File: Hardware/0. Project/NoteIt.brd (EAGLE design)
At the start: 160 x 100 mm, 64 parts, among them CN2 MicroSD Card, CN3 MicroSD Card, CN7 1x4, IC2 MCP73831/2, IC5 S-8261ACMMD-G4MT2U, Q2 SI2374DS, Q3 SI2374DS, Q4 BC817, SW1 KY-040, U10 MSP430FR2476TPTR, U5 TLV75530PDBVR, U6 GL823, U8 ADG774, U9 ADG774, X2 32.768 kHz, X3 microUSB

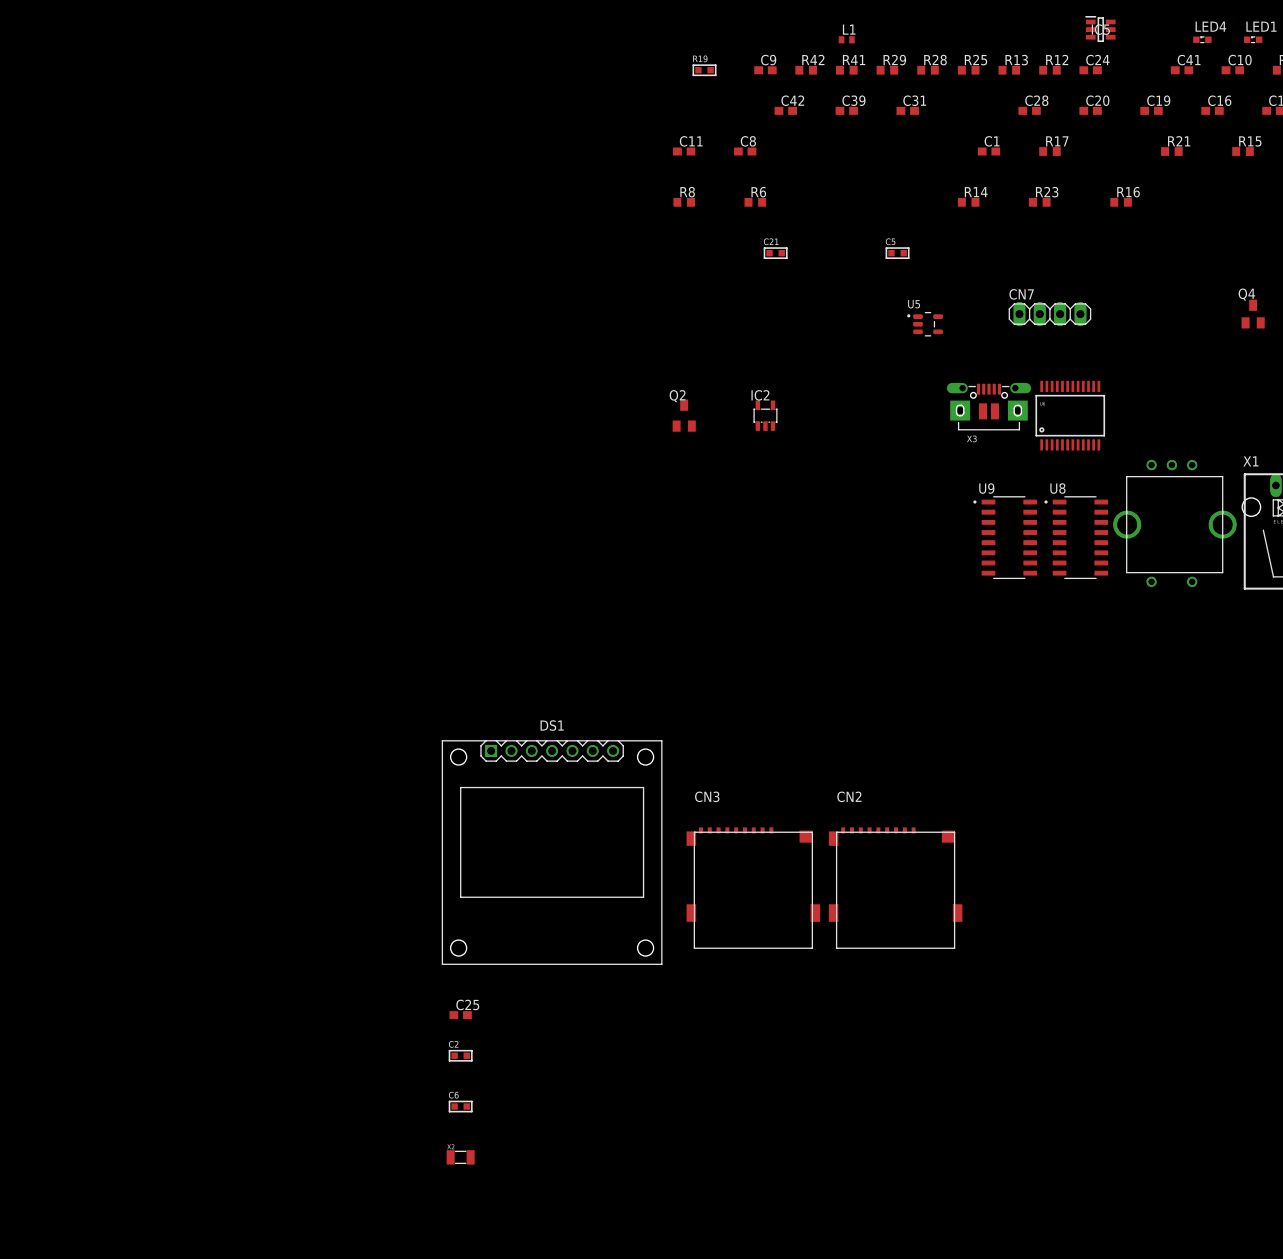
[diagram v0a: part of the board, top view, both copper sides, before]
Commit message: USB/MCU <--> Micro-SD Card Interface added
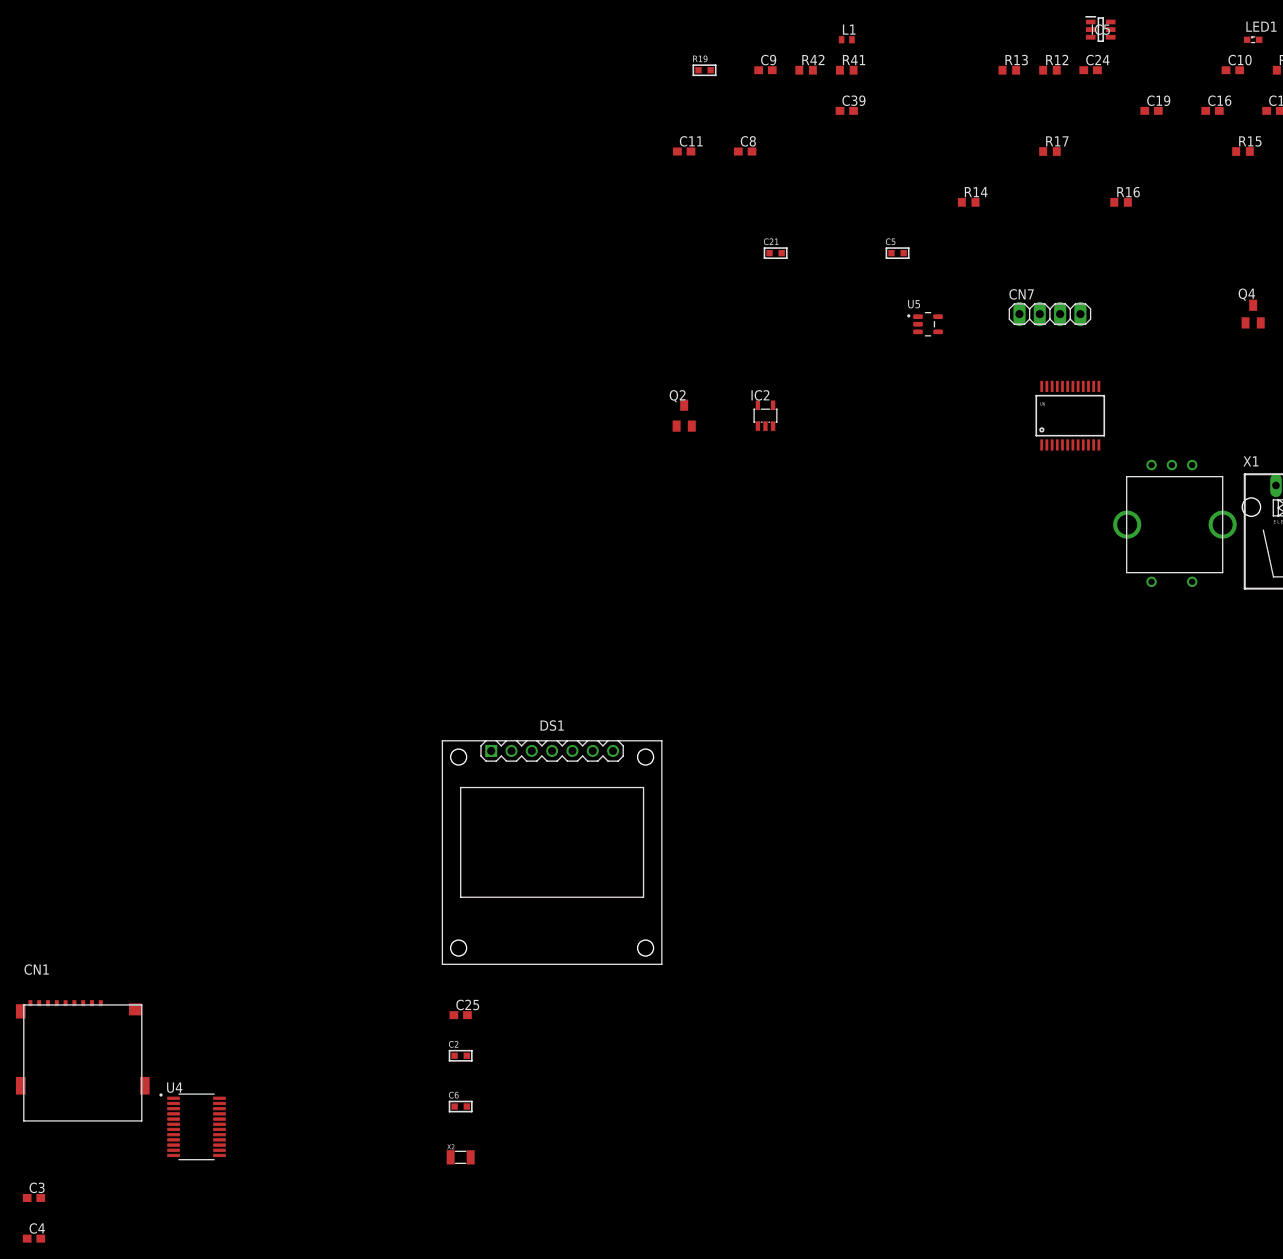
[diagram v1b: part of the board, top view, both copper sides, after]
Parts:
- removed C1, C20, C28, C31, C42: 100nF, rcl:C0603
- removed C41: 10uF, rcl:C0603
- removed CN2, CN3: MicroSD Card, Micro SD:MICROSD-PUSH-OUT
- removed LED4: (no value), led:SML0603
- removed R21, R6, R8: 10k (5%), rcl:R0603
- removed R23: 100k (5%), rcl:R0603
- removed R25: 1k, rcl:R0603
- removed R28, R29: 22R, rcl:R0603
- removed U8, U9: ADG774, ADG774:SOIC127P600X175-16N
- removed X3: microUSB, microbuilder:4UCONN_20329_V2
- added C3, C4: 100nF, rcl:C0603
- added CN1: Micro-SD Card, Micro SD:MICROSD-PUSH-OUT
- added U4: TS3A27518EPWR, TS3A27518EPWR:SOP65P640X120-24N
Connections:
- removed net !SDCARD_SPI_CS!: U8.13
- removed net !SPI_SDCARD_CS: U10.7
- removed net +5V: C1.1, C20.1, C28.1, C31.1, CN2.4, CN3.4, R11.2, R21.2, R6.2, R8.2, U8.16, U9.16
- removed net 5V: IC2.4, R33.2
- removed net MUX_MCU2USB: Q4.C, R11.1, U8.1, U9.1
- removed net N$21: LED4.A, R25.1
- removed net N$22: R28.2, X3.D+
- removed net N$23: R29.2, X3.D-
- removed net N$4: C41.1, C42.1, R25.2, X3.VBUS
- removed net N$6: C41.2, C42.2, LED4.C, X3.BASE@1, X3.BASE@2, X3.GND, X3.SPRT@1, X3.SPRT@2, X3.SPRT@3, X3.SPRT@4
- removed net SDCARD_CLK: CN3.5, U9.7
- removed net SDCARD_CMD/MOSI: CN3.3, R21.1, U9.4
- removed net SDCARD_DAT0/MISO: CN3.7, R6.1, U8.4
- removed net SDCARD_DAT1: CN3.8, U8.7
- removed net SDCARD_DAT2: CN3.1, U8.9
- removed net SDCARD_DAT3/!CS!: CN3.2, U8.12
- removed net SDCARD_SPI_!CS!: CN2.2
- removed net SDCARD_SPI_CLK: U9.6
- removed net SDCARD_SPI_MISO: CN2.7, R23.1, U8.3
- removed net SDCARD_SPI_MOSI: CN2.3, U9.3
- removed net SDCARD_SPI_SCLK: CN2.5
- removed net SPI_SDCARD_CLK: U10.6
- removed net SPI_SDCARD_SIMO: U10.4
- removed net SPI_SDCARD_SOMI: U10.5
- removed net USB_D+: R28.1
- removed net USB_D-: R29.1
- removed net USB_VDD: C16.2, R14.2, R15.1, U6.15, X1.1
- new net !CONNECT_SDCARD_TO_USB: Q4.C, R11.1, U4.14, U4.24
- new net MCU_!SPI_SDCARD_CS: U10.7, U4.16
- new net MCU_SPI_SDCARD_SCLK: U10.6, U4.11
- new net MCU_SPI_SDCARD_SIMO: U10.4, U4.13
- new net MCU_SPI_SDCARD_SOMI: U10.5, U4.15
- new net N$15: CN1.3, U4.6
- new net N$16: CN1.7, U4.7
- new net N$2: CN1.5, U4.4
- new net N$20: CN1.8, U4.9
- new net N$7: CN1.1, U4.10
- new net N$8: CN1.2, U4.12
- new net VUSB: C16.2, IC2.4, R14.2, R15.1, R33.2, U6.15, X1.1
- net !SDCARD_CARD_DETECT!: now also CN1.9; no longer CN2.9, CN3.9, R8.1
- net 0V: now also C3.1, C4.1, CN1.6, CN1.G1, CN1.G2, CN1.G3, CN1.G4, U4.20, U4.5; no longer C1.2, C20.2, C28.2, C31.2, CN2.6, CN2.G1, CN2.G2, CN2.G3, CN2.G4, CN3.6, CN3.G1, CN3.G2, CN3.G3, CN3.G4, R23.2, U8.15, U8.8, U9.15, U9.8
- net 3.3V: now also C3.2, C4.2, CN1.4, R11.2, U4.8
- net USB_CLK: now also U4.2; no longer U9.5
- net USB_CMD: now also U4.1; no longer U9.2
- net USB_DAT0: now also U4.23; no longer U8.2
- net USB_DAT1: now also U4.21; no longer U8.5
- net USB_DAT2: now also U4.19; no longer U8.11
- net USB_DAT3: now also U4.22; no longer U8.14

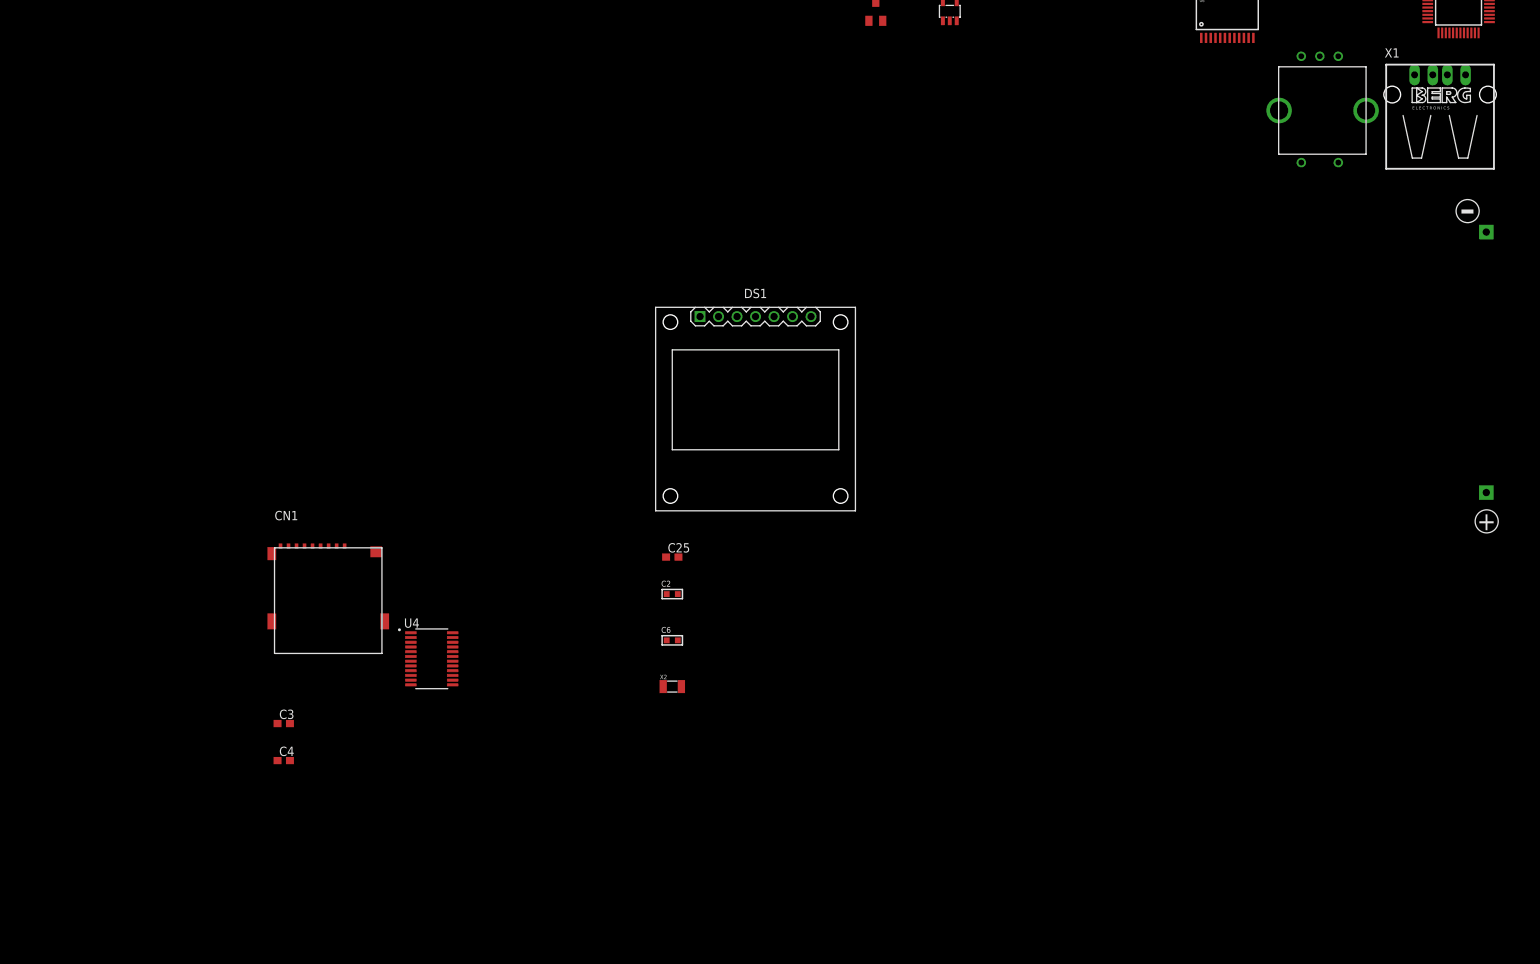
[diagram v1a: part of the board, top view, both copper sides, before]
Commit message: USB C added + UART Rx (datalogger input) level shifter added
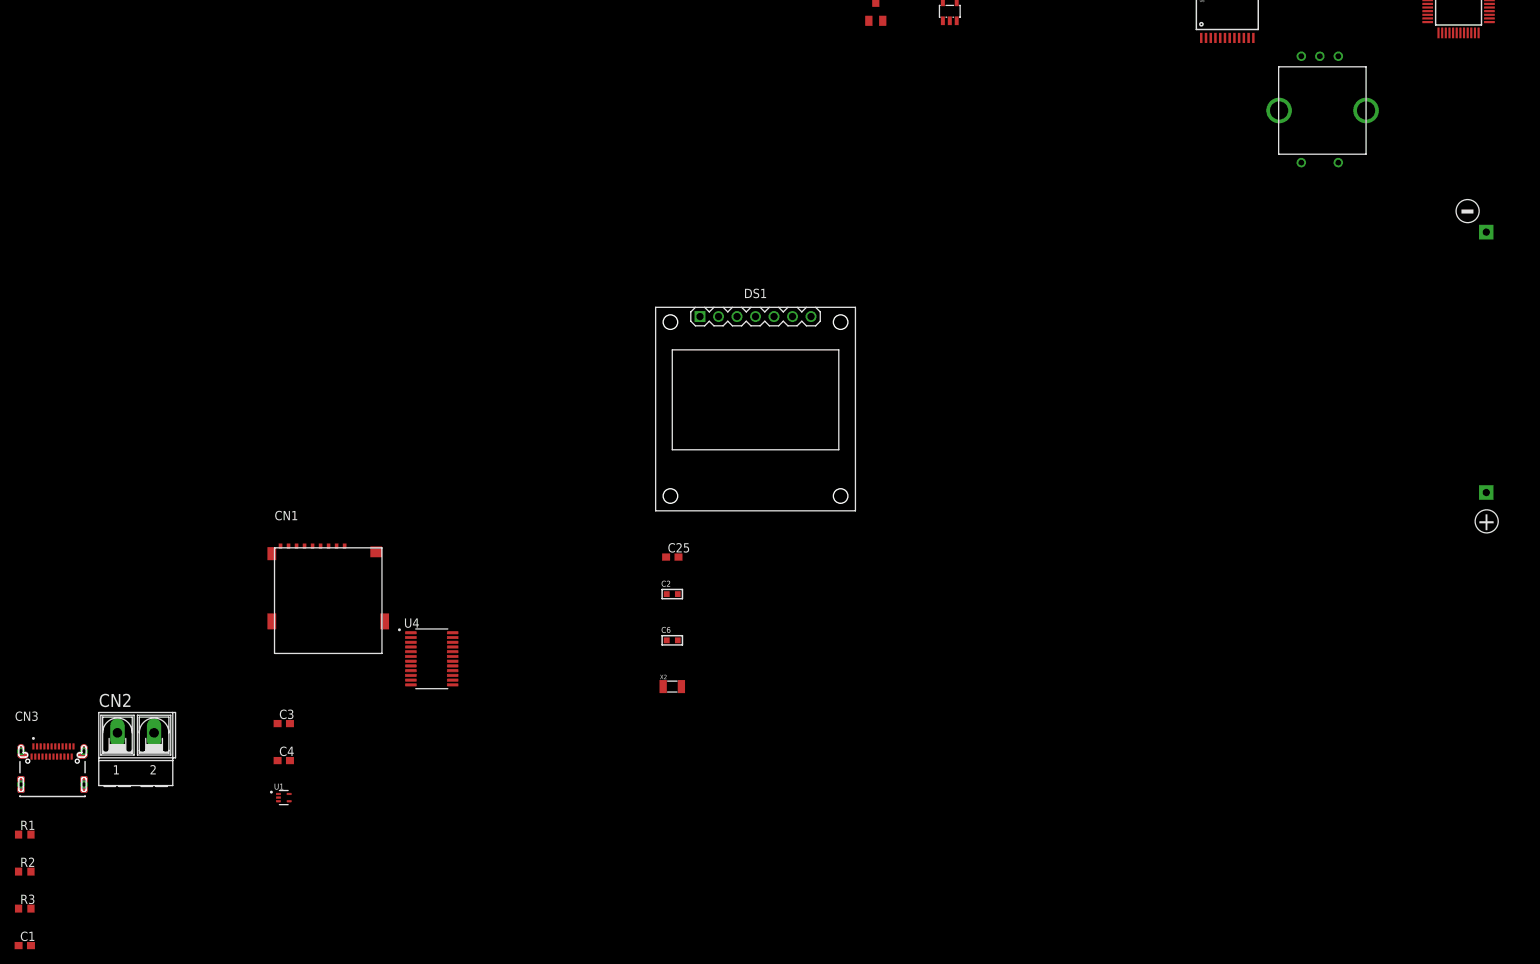
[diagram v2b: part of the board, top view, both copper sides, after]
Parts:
- removed X1: (no value), con-berg:PN87520
- added C1: 4.7nF, rcl:C0603
- added CN2: (no value), con-ptr500:AK500/2-H
- added CN3: USB 3.2 Gen 2 Type C Receptacle, USB C CONNECOTR:GCT_USB4080-03-A_REVA
- added R1, R2: 5k1 (5%), rcl:R0603
- added R3: 1M, rcl:R0603
- added U1: SN74AHC1G125DRLR, SN74AHC1G125DRLR:SOT-553
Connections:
- removed net N$11: U6.19, X1.3
- new net N$21: CN3.B5, R2.1
- new net N$4: CN2.1, U1.2
- new net N$6: CN3.A5, R1.1
- new net USB_N: CN3.A7, CN3.B7, U6.18
- new net USB_P: CN3.A6, CN3.B6, U6.19
- net 0V: now also C1.1, CN2.2, CN3.A1, CN3.A12, CN3.B1, CN3.B12, R1.2, R2.2, R3.2, U1.1, U1.3; no longer X1.4
- net 3.3V: now also U1.5
- net N$10: now also C1.2, CN3.G1, CN3.G2, CN3.G3, CN3.G4, R3.1; no longer U6.18, X1.2
- net UART_DATALOGGER_RX: now also U1.4
- net VUSB: now also CN3.A4, CN3.A9, CN3.B4, CN3.B9; no longer X1.1

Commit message: SD-Card to USB IC (GL823K) package updated
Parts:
- removed C12: 100nF, rcl:C0603
- removed C23: 1nF x 50V, My-RLC:C0603
- removed CN7: 1x4, pinhead:1X04
- removed L1: (no value), inductors:0402
- removed LED1: (no value), led:SML0603
- removed R16: 680R (5%), rcl:R0603
- removed R19: 47k (5%), My-RLC:R0603
- removed R33: 470R, rcl:R0603
- removed U6: GL823, GL823:SSOP24
- added C13: 1nF x 50V, My-RLC:C0603
- added C14: 100nF, rcl:C0805
- added C7: 100nF, rcl:C0603
- added CN4: ARM 10-pin JTAG Connector, SamacSys_Parts:FTSH10501LDVKTR
- added G1: CR1220, battery:CH291-1220LF
- added R10: 4k7, rcl:R0603
- added R18: 10k, rcl:R0603
- added R4, R9: 100k, rcl:R0603
- added R5: 10k (5%), rcl:R0603
- added R6, R7, R8: 47k (5%), My-RLC:R0603
- added U2: GL823K, SamacSys_Parts:SOP64P600X175-16N
- added U8: DS3231/SO, adafruit:SO16W
- C10: value 10uF -> 4.7uF
- C11, C15: value 100nF -> 4.7uF
- moved C10 353.1 mm to (-252.7, -158.8)
- moved C11 310.0 mm to (-252.7, -163.8)
- moved CN1 63.8 mm to (-233.7, -38.1)
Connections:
- net !GPIO_OLED_RESET renamed !GPIO_DISPLAY_RESET
- net GPIO_OLED_TRANSMISSION_MODE renamed GPIO_DISPLAY_TRANSMISSION_MODE
- removed net ADC_VBAT: R41.1, R42.2
- removed net GPIO_EXTERNAL_SUPPLY_DETECT: U10.42
- removed net GPIO_SDCARD_DETECT: U10.18
- removed net N$18: R16.1, U6.20
- removed net N$19: L1.2, U6.21
- removed net N$24: LED1.A, R33.1
- removed net N$25: IC2.1, LED1.C
- removed net N$9 (its old number): C12.2, U6.7
- removed net OLED_SPI_!CS!: DS1.7
- removed net OLED_SPI_MOSI: DS1.4
- removed net OLED_SPI_SCLK: DS1.3
- removed net SPI_DISPLAY_CLK: U10.10
- removed net SPI_DISPLAY_SOMI: U10.8
- new net GPIO_BATTERY_CHARGING_STATUS: IC2.1, U10.42
- new net N$13: C15.2, U2.8
- new net N$22: G1.+, U8.14
- new net SPI_DISPLAY_SCLK: DS1.3, U10.10
- net !SDCARD_CARD_DETECT!: now also R5.2, U10.18; no longer U6.1
- net !SPI_DISPLAY_CS: now also DS1.7
- net 0V: now also C13.2, C14.1, CN4.3, CN4.5, CN4.7, CN4.9, G1.-, R18.1, R9.1, U2.1, U2.14, U8.10, U8.11, U8.12, U8.13, U8.5, U8.6, U8.7, U8.8, U8.9; no longer C10.1, C11.1, C12.1, C23.2, CN7.1, LED2.C, R16.2, U6.12, U6.13, U6.16, U6.17, U6.22, U6.24, U6.5
- net 3.3V: now also C14.2, CN4.1, R5.1, R6.1, R7.1, R8.1, U8.2; no longer CN7.4, R19.1
- net ADC_BATTERY_VOLTAGE: now also R41.1, R42.2
- net GPIO_USB_DETECT: now also R4.1, R9.2
- net I2C_RTC_SCL: now also R8.2, U8.16
- net I2C_RTC_SDA: now also R7.2, U8.15
- net ICSP_SBWTCK: now also CN4.4; no longer CN7.2
- net ICSP_SBWTDIO: now also C13.1, CN4.6, R6.2; no longer C23.1, CN7.3, R19.2
- net N$12: now also R10.1, R18.2, U2.11; no longer R17.1, U6.11
- net N$17: now also C10.2, C11.2, R10.2, R17.1, U2.13, U2.9; no longer C15.2, U6.23
- net N$5: now also LED2.C, U2.12; no longer C10.2, C11.2, L1.1, U6.14, U6.6
- net SPI_DISPLAY_SIMO: now also DS1.4
- net USB_CLK: now also U2.4; no longer U6.4
- net USB_CMD: now also U2.5; no longer U6.8
- net USB_DAT0: now also U2.3; no longer U6.3
- net USB_DAT1: now also U2.2; no longer U6.2
- net USB_DAT2: now also U2.7; no longer U6.10
- net USB_DAT3: now also U2.6; no longer U6.9
- net USB_N: now also U2.16; no longer U6.18
- net USB_P: now also U2.15; no longer U6.19
- net VUSB: now also R4.2, U2.10; no longer R33.2, U6.15
- net XTAL_IN: now also U10.46; no longer U10.47
- net XTAL_OUT: now also U10.47; no longer U10.46

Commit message: PCB layout init
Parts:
- C1: value 4.7nF -> (none)
- C10, C11, C15: value 4.7uF -> (none)
- C13: value 1nF x 50V -> (none)
- C14, C16, C19, C25, C3, C39, C4, C7, C8: value 100nF -> (none)
- C2, C6: value 22pF x 100V -> (none)
- C21: value 10uF x 10V -> (none)
- C24, C9: value 1uF -> (none)
- C5: value 100nF x 50V -> (none)
- CN1: value Micro-SD Card -> (none)
- CN3: value USB 3.2 Gen 2 Type C Receptacle -> (none)
- CN4: value ARM 10-pin JTAG Connector -> (none)
- DS1: value SSD1306 -> (none)
- G1: value CR1220 -> (none)
- IC2: value MCP73831/2 -> (none)
- IC5: value S-8261ACMMD-G4MT2U -> (none)
- Q2, Q3: value SI2374DS -> (none)
- Q4: value BC817 -> (none)
- R1, R2: value 5k1 (5%) -> (none)
- R10: value 4k7 -> (none)
- R11, R15, R5: value 10k (5%) -> (none)
- R12: value 4K7 -> (none)
- R13: value 2k -> (none)
- R14: value 4K7 (5%) -> (none)
- R17: value 1k (5%) -> (none)
- R18: value 10k -> (none)
- R22: value 470R -> (none)
- R3, R41, R42: value 1M -> (none)
- R4, R9: value 100k -> (none)
- R6, R7, R8: value 47k (5%) -> (none)
- U1: value SN74AHC1G125DRLR -> (none)
- U10: value MSP430FR2476TPTR -> (none)
- U2: value GL823K -> (none)
- U4: value TS3A27518EPWR -> (none)
- U5: value TLV75530PDBVR -> (none)
- U8: value DS3231/SO -> (none)
- X2: value 32.768 kHz -> (none)
- moved U8 308.9 mm to (38.1, 7.62), flipped to the bottom, turned to 180 degrees
- moved U2 294.3 mm to (-5.71, 26.7), flipped to the bottom, turned to 180 degrees
- moved C10 288.8 mm to (-29.2, 24.1)
- moved C11 288.8 mm to (-29.2, 19.1)
- moved C7 288.8 mm to (-29.2, 29.2)
- moved R10 288.8 mm to (-29.2, 39.4)
- moved R18 288.8 mm to (-29.2, 34.3)
- moved R4 288.8 mm to (-29.2, 57.1)
- moved R7 288.8 mm to (-29.2, 67.3)
- moved R8 288.8 mm to (-29.2, 62.2)
- moved R9 288.8 mm to (-29.2, 52.1)
- moved G1 284.2 mm to (17.8, 9.53), flipped to the bottom, turned to 270 degrees
- moved CN4 275.1 mm to (25.0, 6.35), turned to 180 degrees
- moved C13 260.5 mm to (-38.7, 73.7)
- moved R6 260.5 mm to (-31.1, 72.4)
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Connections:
- removed net N$17: C10.2, C11.2, R10.2, R17.1, U2.13, U2.9
- new net N$11: C10.2, C11.2, R10.1, R17.1, U2.13, U2.9
- net 0V: now also C10.1, C11.1, C7.1
- net N$12: now also R10.2; no longer R10.1
- net VUSB: now also C7.2
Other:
- board size 160 x 100 mm -> 50 x 50 mm
